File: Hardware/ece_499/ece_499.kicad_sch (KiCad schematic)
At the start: 21 parts, among them Q1 DMN2004WK, Q2 DMN2004WK, Q3 DMN2004WK, Q4 DMN2004WK, SW1 RotaryEncoder_Switch, U1 Xiao ESP32-C3, U2 ATA6561-GAQW-N, U3 AP62200WU-7, U4 I2C_LCD

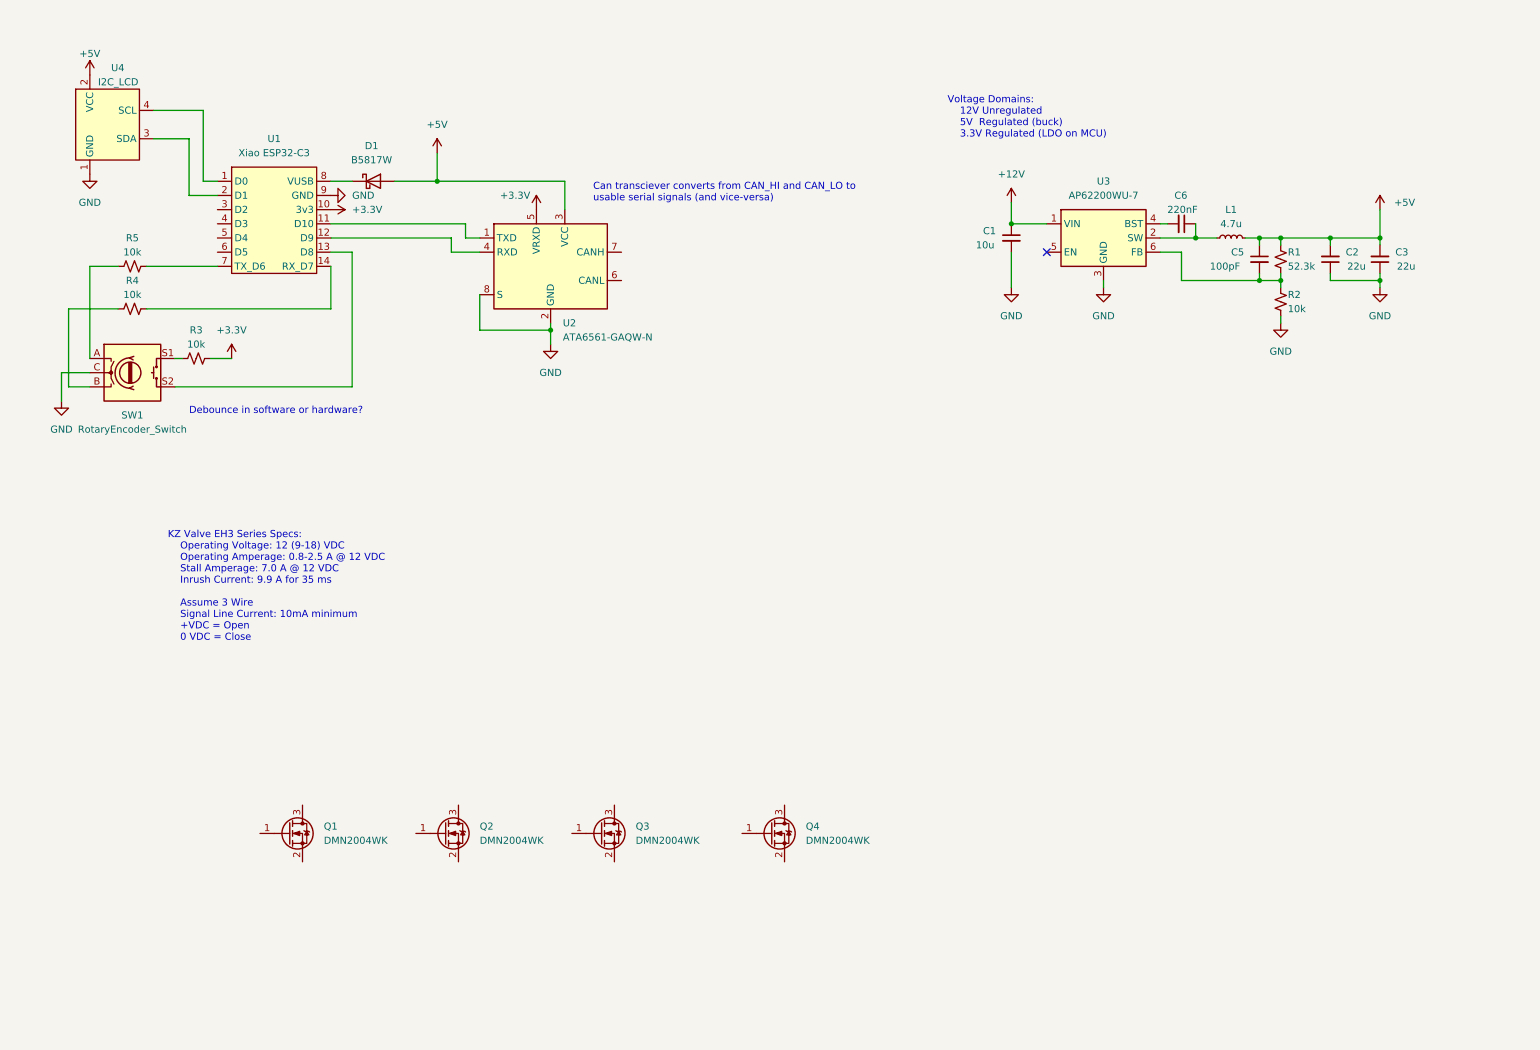
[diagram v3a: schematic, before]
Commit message: Design connectors for connectors to actuators
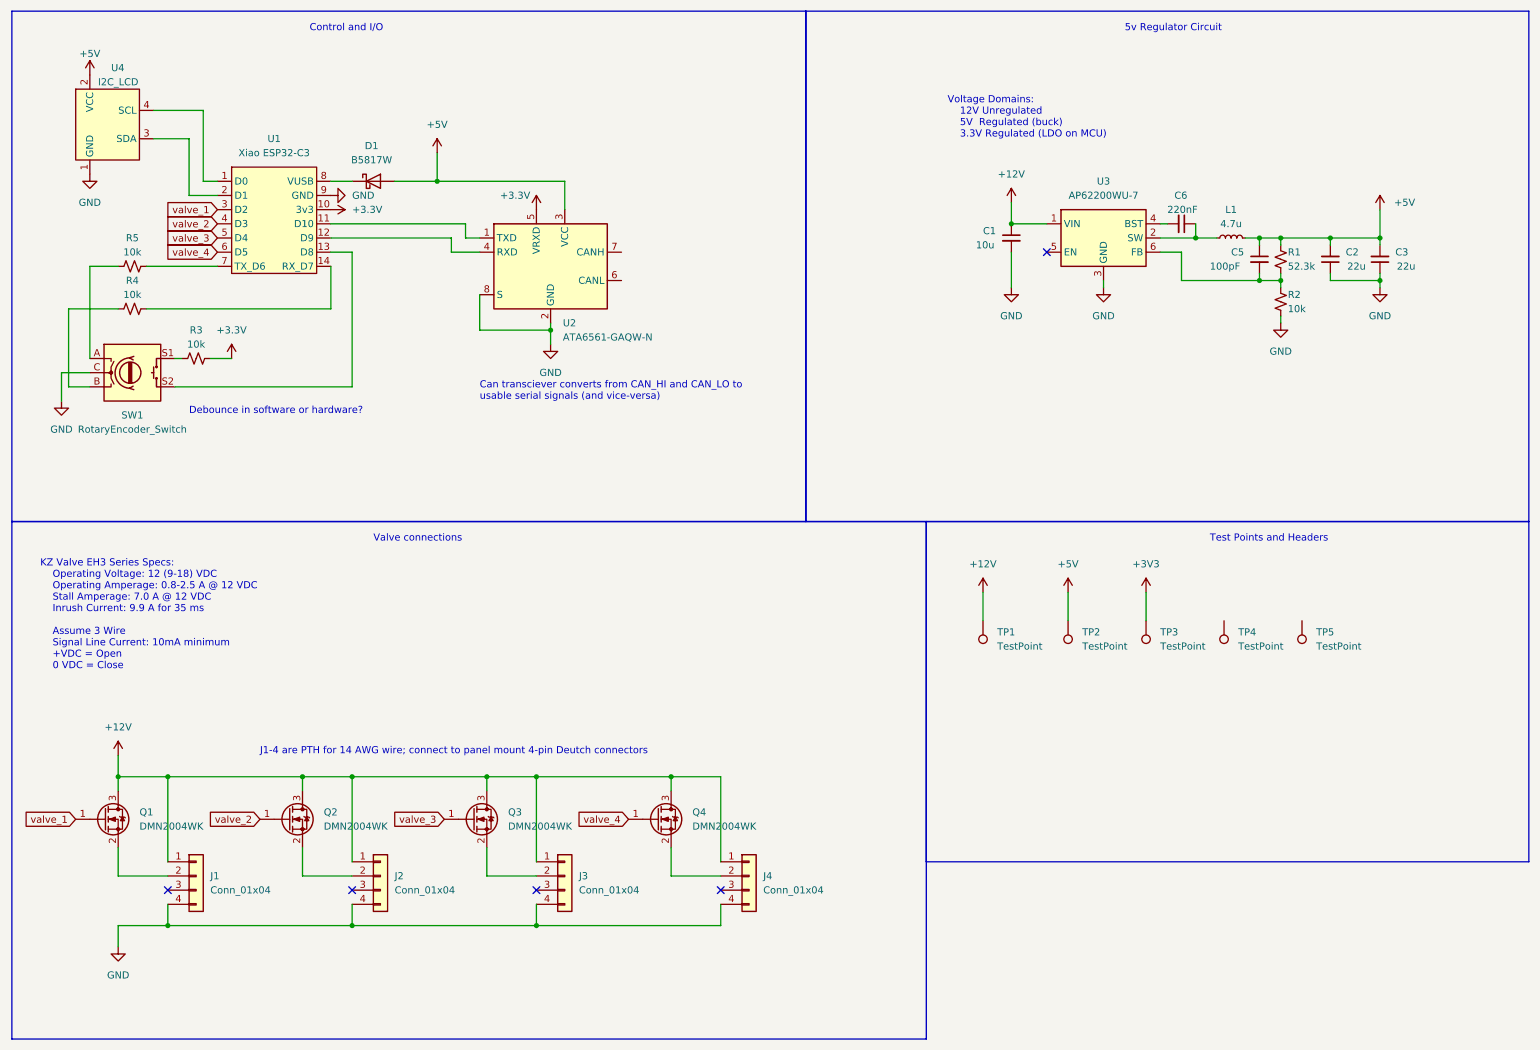
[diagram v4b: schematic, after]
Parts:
- added J1, J2, J3, J4: Conn_01x04, symbol Connector_Generic:Conn_01x04
- added TP1, TP2, TP3, TP4, TP5: TestPoint, symbol Connector:TestPoint
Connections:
- net +12V: now also Q1.3 (D), Q2.3 (D), Q3.3 (D), Q4.3 (D), J1.1 (Pin_1), J2.1 (Pin_1), J3.1 (Pin_1), J4.1 (Pin_1), TP1.1
- net +5V: now also TP2.1
- net GND: now also J1.4 (Pin_4), J2.4 (Pin_4), J3.4 (Pin_4), J4.4 (Pin_4)
- net valve_1: now reaches U1.3 (D2)
- net valve_1: now also Q1.1 (G)
- net valve_2: now reaches U1.4 (D3)
- net valve_2: now also Q2.1 (G)
- net valve_3: now reaches U1.5 (D4)
- net valve_3: now also Q3.1 (G)
- net valve_4: now reaches U1.6 (D5)
- net valve_4: now also Q4.1 (G)
- net at Q1.2 (S): now also J1.2 (Pin_2)
- net at Q3.2 (S): now also J3.2 (Pin_2)
- net at Q4.2 (S): now also J4.2 (Pin_2)
- net at Q2.2 (S): now also J2.2 (Pin_2)
- new net +3V3: TP3.1
- no-connect marks 1 -> 5
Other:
- note added: "5v Regulator Circuit"
- note added: "Control and I/O"
- note added: "J1-4 are PTH for 14 AWG wire; connect to panel mount 4-pin Deutch connectors"
- note added: "Test Points and Headers"
- note added: "Valve connections"
- moved on the sheet: Q1, Q2, Q3, Q4

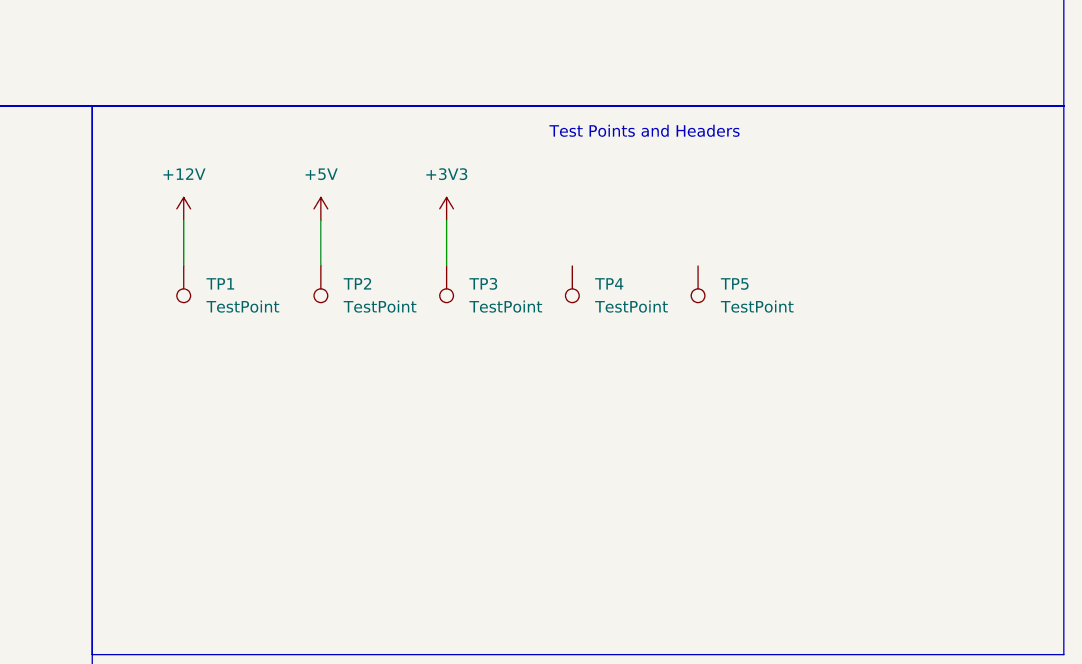
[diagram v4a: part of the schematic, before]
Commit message: Add more test points
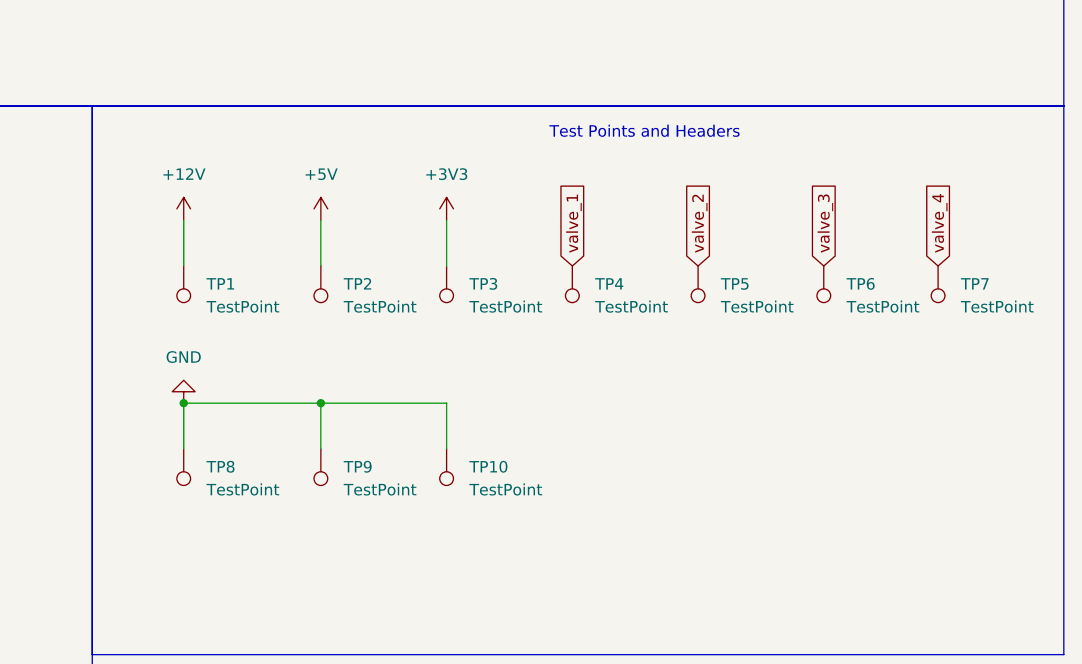
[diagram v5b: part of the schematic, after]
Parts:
- added TP10, TP6, TP7, TP8, TP9: TestPoint, symbol Connector:TestPoint
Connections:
- net GND: now also TP10.1, TP8.1, TP9.1
- net valve_1: now also TP4.1
- net valve_2: now also TP5.1
- net valve_3: now also TP6.1
- net valve_4: now also TP7.1
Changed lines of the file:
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@@
   (junction (at 73.66 176.53) (diameter 0) (color 0 0 0 0)
   )
+  (junction (at 186.69 137.16) (diameter 0) (color 0 0 0 0)
+  )
   (junction (at 240.03 60.96) (diameter 0) (color 0 0 0 0)
+  )
+  (junction (at 201.93 137.16) (diameter 0) (color 0 0 0 0)
   )
   (no_connect (at 40.64 170.18))
@@
     (stroke (width 0) (type default))
   )
+  (wire (pts (xy 215.9 137.16) (xy 215.9 142.24))
+    (stroke (width 0) (type default))
+  )
   (wire (pts (xy 44.45 35.56) (xy 44.45 45.72))
     (stroke (width 0) (type default))
@@
     (stroke (width 0) (type default))
   )
+  (wire (pts (xy 186.69 137.16) (xy 186.69 142.24))
+    (stroke (width 0) (type default))
+  )
   (wire (pts (xy 31.75 180.34) (xy 31.75 176.53))
     (stroke (width 0) (type default))
@@
     (stroke (width 0) (type default))
   )
+  (wire (pts (xy 186.69 137.16) (xy 201.93 137.16))
+    (stroke (width 0) (type default))
+  )
   (wire (pts (xy 88.9 38.1) (xy 88.9 43.18))
     (stroke (width 0) (type default))
@@
   )
   (wire (pts (xy 40.64 149.86) (xy 64.77 149.86))
+    (stroke (width 0) (type default))
+  )
+  (wire (pts (xy 201.93 137.16) (xy 201.93 142.24))
+    (stroke (width 0) (type default))
+  )
+  (wire (pts (xy 201.93 137.16) (xy 215.9 137.16))
     (stroke (width 0) (type default))
   )
@@
     )
   )
+  (global_label "valve_2" (shape input) (at 243.84 121.92 90) (fields_autoplaced)
+    (effects (font (size 1.27 1.27)) (justify left))
+    (property "Intersheetrefs" "${INTERSHEET_REFS}" (at 243.84 111.9197 90)
+      (effects (font (size 1.27 1.27)) (justify left) hide)
+    )
+  )
   (global_label "valve_1" (shape input) (at 24.13 157.48 180) (fields_autoplaced)
     (effects (font (size 1.27 1.27)) (justify right))
@@
     )
   )
+  (global_label "valve_1" (shape input) (at 229.87 121.92 90) (fields_autoplaced)
+    (effects (font (size 1.27 1.27)) (justify left))
+    (property "Intersheetrefs" "${INTERSHEET_REFS}" (at 229.87 111.9197 90)
+      (effects (font (size 1.27 1.27)) (justify left) hide)
+    )
+  )
   (global_label "valve_3" (shape input) (at 90.17 157.48 180) (fields_autoplaced)
     (effects (font (size 1.27 1.27)) (justify right))
@@
     )
   )
+  (global_label "valve_4" (shape input) (at 270.51 121.92 90) (fields_autoplaced)
+    (effects (font (size 1.27 1.27)) (justify left))
+    (property "Intersheetrefs" "${INTERSHEET_REFS}" (at 270.51 111.9197 90)
+      (effects (font (size 1.27 1.27)) (justify left) hide)
+    )
+  )
   (global_label "valve_4" (shape input) (at 123.19 157.48 180) (fields_autoplaced)
     (effects (font (size 1.27 1.27)) (justify right))
@@
     )
   )
+  (global_label "valve_3" (shape input) (at 257.81 121.92 90) (fields_autoplaced)
+    (effects (font (size 1.27 1.27)) (justify left))
+    (property "Intersheetrefs" "${INTERSHEET_REFS}" (at 257.81 111.9197 90)
+      (effects (font (size 1.27 1.27)) (justify left) hide)
+    )
+  )
   (symbol (lib_id "power:+12V") (at 186.69 116.84 0) (unit 1)
     (in_bom yes) (on_board yes) (dnp no) (fields_autoplaced)
@@
         (path "/3f2f140e-ca1f-4768-bf63-ce27bfebd1d1"
           (reference "C1") (unit 1)
+        )
+      )
+    )
+  )
+  (symbol (lib_id "power:GND") (at 186.69 137.16 180) (unit 1)
+    (in_bom yes) (on_board yes) (dnp no) (fields_autoplaced)
+    (property "Reference" "#PWR021" (at 186.69 130.81 0)
+      (effects (font (size 1.27 1.27)) hide)
+    )
+    (property "Value" "GND" (at 186.69 132.08 0)
+      (effects (font (size 1.27 1.27)))
+    )
+    (property "Footprint" "" (at 186.69 137.16 0)
+      (effects (font (size 1.27 1.27)) hide)
+    )
+    (property "Datasheet" "" (at 186.69 137.16 0)
+      (effects (font (size 1.27 1.27)) hide)
+    )
+    (pin "1")
+    (instances
+      (project "ece_499"
+        (path "/3f2f140e-ca1f-4768-bf63-ce27bfebd1d1"
+          (reference "#PWR021") (unit 1)
         )
       )
@@
     )
   )
+  (symbol (lib_id "Connector:TestPoint") (at 201.93 142.24 180) (unit 1)
+    (in_bom yes) (on_board yes) (dnp no) (fields_autoplaced)
+    (property "Reference" "TP9" (at 204.47 144.272 0)
+      (effects (font (size 1.27 1.27)) (justify right))
+    )
+    (property "Value" "TestPoint" (at 204.47 146.812 0)
+      (effects (font (size 1.27 1.27)) (justify right))
+    )
+    (property "Footprint" "" (at 196.85 142.24 0)
+      (effects (font (size 1.27 1.27)) hide)
+    )
+    (property "Datasheet" "~" (at 196.85 142.24 0)
+      (effects (font (size 1.27 1.27)) hide)
+    )
+    (pin "1")
+    (instances
+      (project "ece_499"
+        (path "/3f2f140e-ca1f-4768-bf63-ce27bfebd1d1"
+          (reference "TP9") (unit 1)
+        )
+      )
+    )
+  )
   (symbol (lib_id "Device:C_Small") (at 222.25 50.8 270) (unit 1)
     (in_bom yes) (on_board yes) (dnp no)
@@
         (path "/3f2f140e-ca1f-4768-bf63-ce27bfebd1d1"
           (reference "C6") (unit 1)
+        )
+      )
+    )
+  )
+  (symbol (lib_id "Connector:TestPoint") (at 186.69 142.24 180) (unit 1)
+    (in_bom yes) (on_board yes) (dnp no) (fields_autoplaced)
+    (property "Reference" "TP8" (at 189.23 144.272 0)
+      (effects (font (size 1.27 1.27)) (justify right))
+    )
+    (property "Value" "TestPoint" (at 189.23 146.812 0)
+      (effects (font (size 1.27 1.27)) (justify right))
+    )
+    (property "Footprint" "" (at 181.61 142.24 0)
+      (effects (font (size 1.27 1.27)) hide)
+    )
+    (property "Datasheet" "~" (at 181.61 142.24 0)
+      (effects (font (size 1.27 1.27)) hide)
+    )
+    (pin "1")
+    (instances
+      (project "ece_499"
+        (path "/3f2f140e-ca1f-4768-bf63-ce27bfebd1d1"
+          (reference "TP8") (unit 1)
         )
       )
@@
     )
   )
+  (symbol (lib_id "Connector:TestPoint") (at 257.81 121.92 180) (unit 1)
+    (in_bom yes) (on_board yes) (dnp no) (fields_autoplaced)
+    (property "Reference" "TP6" (at 260.35 123.952 0)
+      (effects (font (size 1.27 1.27)) (justify right))
+    )
+    (property "Value" "TestPoint" (at 260.35 126.492 0)
+      (effects (font (size 1.27 1.27)) (justify right))
+    )
+    (property "Footprint" "" (at 252.73 121.92 0)
+      (effects (font (size 1.27 1.27)) hide)
+    )
+    (property "Datasheet" "~" (at 252.73 121.92 0)
+      (effects (font (size 1.27 1.27)) hide)
+    )
+    (pin "1")
+    (instances
+      (project "ece_499"
+        (path "/3f2f140e-ca1f-4768-bf63-ce27bfebd1d1"
+          (reference "TP6") (unit 1)
+        )
+      )
+    )
+  )
   (symbol (lib_id "Connector:TestPoint") (at 215.9 121.92 180) (unit 1)
     (in_bom yes) (on_board yes) (dnp no) (fields_autoplaced)
@@
     )
   )
+  (symbol (lib_id "Connector:TestPoint") (at 215.9 142.24 180) (unit 1)
+    (in_bom yes) (on_board yes) (dnp no) (fields_autoplaced)
+    (property "Reference" "TP10" (at 218.44 144.272 0)
+      (effects (font (size 1.27 1.27)) (justify right))
+    )
+    (property "Value" "TestPoint" (at 218.44 146.812 0)
+      (effects (font (size 1.27 1.27)) (justify right))
+    )
+    (property "Footprint" "" (at 210.82 142.24 0)
+      (effects (font (size 1.27 1.27)) hide)
+    )
+    (property "Datasheet" "~" (at 210.82 142.24 0)
+      (effects (font (size 1.27 1.27)) hide)
+    )
+    (pin "1")
+    (instances
+      (project "ece_499"
+        (path "/3f2f140e-ca1f-4768-bf63-ce27bfebd1d1"
+          (reference "TP10") (unit 1)
+        )
+      )
+    )
+  )
   (symbol (lib_id "power:+3V3") (at 215.9 116.84 0) (unit 1)
     (in_bom yes) (on_board yes) (dnp no) (fields_autoplaced)
@@
         )
       )
+    )
+  )
+  (symbol (lib_id "Connector:TestPoint") (at 270.51 121.92 180) (unit 1)
+    (in_bom yes) (on_board yes) (dnp no) (fields_autoplaced)
+    (property "Reference" "TP7" (at 273.05 123.952 0)
+      (effects (font (size 1.27 1.27)) (justify right))
+    )
+    (property "Value" "TestPoint" (at 273.05 126.492 0)
+      (effects (font (size 1.27 1.27)) (justify right))
+    )
+    (property "Footprint" "" (at 265.43 121.92 0)
+      (effects (font (size 1.27 1.27)) hide)
+    )
+    (property "Datasheet" "~" (at 265.43 121.92 0)
+      (effects (font (size 1.27 1.27)) hide)
+    )
+    (pin "1")
+    (instances
+      (project "ece_499"
+        (path "/3f2f140e-ca1f-4768-bf63-ce27bfebd1d1"
+          (reference "TP7") (unit 1)
+        )
+      )
